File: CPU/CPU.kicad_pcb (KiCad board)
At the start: 2 copper layers, 157.1 x 85.3 mm, 88 parts, among them J101 Conn_02x10_Odd_Even, J102 Conn_02x14_Odd_Even_MountingP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, J301 Conn_02x03_Odd_Even, J302 1X4SMD-FPC, J303 Conn_02x03_Odd_Even, Q101 IRLML0040TR, Q102 IRLML0040TR, Q201 DMC4050, Q301 IRLML0040TR, Q302 IRLML0040TR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

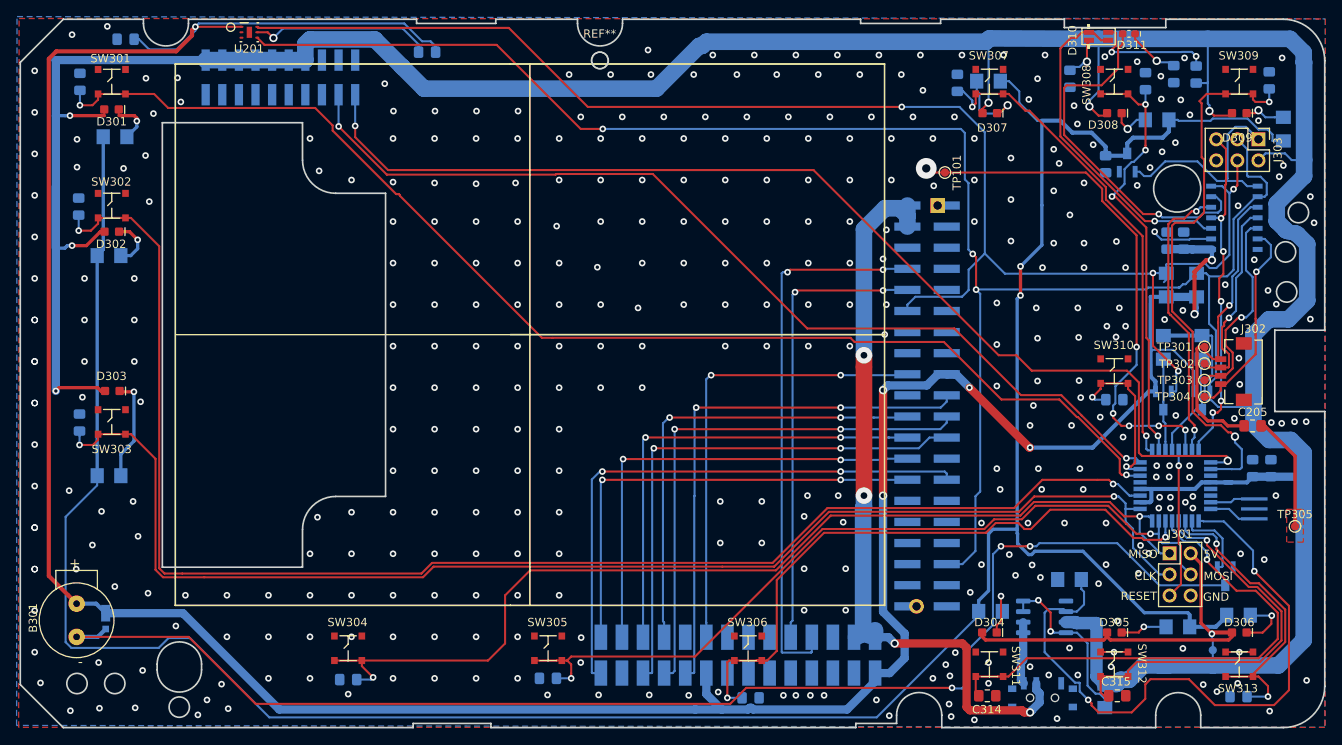
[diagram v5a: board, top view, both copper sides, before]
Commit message: Updates from CPU v1 were completed. Switched out Tiny84 for a tiny1614 because the 84 lacks a hardware twi driver. This version was sent to production at jlcpcb.
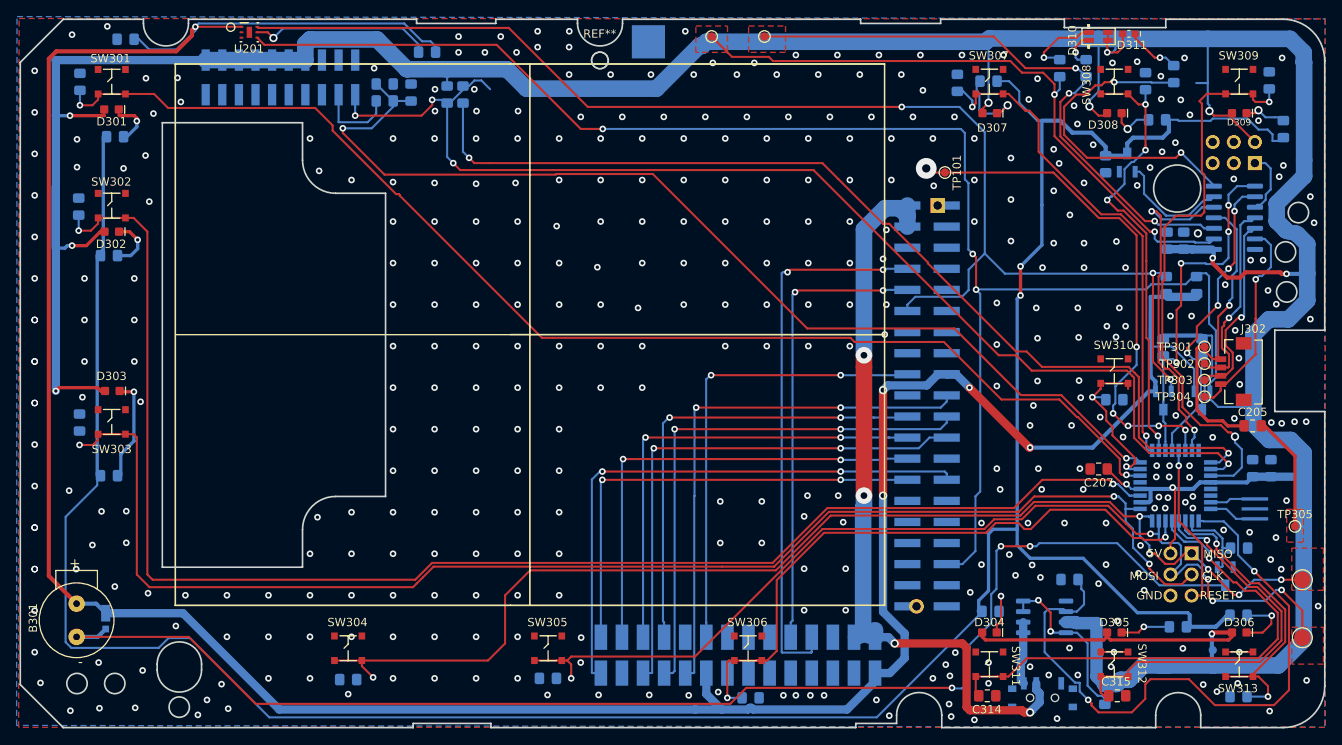
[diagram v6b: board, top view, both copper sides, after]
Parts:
- added C206: 100pF, Capacitor_SMD:C_0805_2012Metric_Pad1.15x1.40mm_HandSolder, B.Cu at (77.5, 54.4)
- added C207: 100nF, Capacitor_SMD:C_0805_2012Metric_Pad1.15x1.40mm_HandSolder, F.Cu at (160.3, 99.7)
- added D201: Schottky, Diode_SMD:D_0805_2012Metric_Pad1.15x1.40mm_HandSolder, B.Cu at (74.3, 53.3)
- added R202: 390K, Resistor_SMD:R_0805_2012Metric_Pad1.15x1.40mm_HandSolder, B.Cu at (81.8, 54.6)
- added R203: 2K, Resistor_SMD:R_0805_2012Metric_Pad1.15x1.40mm_HandSolder, B.Cu at (83.7, 54.6)
- added R204: 1K, Resistor_SMD:R_0805_2012Metric_Pad1.15x1.40mm_HandSolder, B.Cu at (74.3, 55.4)
- added R205: 10K, Resistor_SMD:R_0805_2012Metric_Pad1.15x1.40mm_HandSolder, B.Cu at (177.2, 109.2)
- added RX301: TestPoint, TestPoint:TestPoint_Pad_D1.0mm, F.Cu at (120.0, 47.6)
- added TP201: TestPoint, TestPoint:TestPoint_Pad_4.0x4.0mm, B.Cu at (106.0, 48.3)
- added TPRX201: TestPoint, TestPoint:TestPoint_Pad_D2.0mm, F.Cu at (184.8, 113.0)
- added TPTX201: TestPoint, TestPoint:TestPoint_Pad_D2.0mm, F.Cu at (184.8, 120.0)
- added TX301: TestPoint, TestPoint:TestPoint_Pad_D1.0mm, F.Cu at (113.7, 47.6)
- J301, J303: moved to B.Cu
- R101, R102, R103, R104, R208, R209, R301, R302, R303, R304, R305, R306, R307, R308, R309: footprint CPU:R1206 -> Resistor_SMD:R_0805_2012Metric_Pad1.15x1.40mm_HandSolder
- U202: value ATTINY84ATTINY84-20PU -> ATtiny1614-SS; footprint MarcoK:14SOIC -> Package_SO:SOIC-14_3.9x8.7mm_P1.27mm
- moved R310 16.4 mm to (155.6, 51.4), turned to 90 degrees
- moved J303 2.90 mm to (179.1, 62.9), turned to 90 degrees
- moved J301 2.65 mm to (171.4, 109.9), turned to 180 degrees
- moved R311 2.33 mm to (158.8, 51.4)
- moved Y301 0.07 mm to (179.1, 104.5)
- turned U202 to 0 degrees
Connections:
- C202 pad 1: +3V3 -> 5V
- C203 pad 2: +3V3 -> 5V
- C306 pad 1: GND -> Net-(C306-Pad1)
- C306 pad 2: /Micro Controller Devices/SW- -> Net-(C306-Pad2)
- C307 pad 1: GND -> Net-(C307-Pad1)
- C307 pad 2: /Micro Controller Devices/SWA -> Net-(C307-Pad2)
- C308 pad 1: GND -> Net-(C308-Pad1)
- C308 pad 2: /Micro Controller Devices/SWB -> Net-(C308-Pad2)
- J303 pad 1: /I2C Devices/LED_PWM -> /I2C Devices/UPDI
- J303 pad 3: /SCL -> Net-(J303-Pad3)
- J303 pad 4: /SDA -> Net-(J303-Pad4)
- J303 pad 5: /I2C Devices/85RES -> Net-(J303-Pad5)
- R310 pad 1: /I2C Devices/GREEN -> /I2C Devices/RED
- R311 pad 2: /I2C Devices/RED -> /I2C Devices/GREEN
- U202 pad 1: +3V3 -> 5V
- U202 pad 10: /I2C Devices/SCC -> /I2C Devices/UPDI
- U202 pad 2: /I2C Devices/GREEN -> /I2C Devices/RED
- U202 pad 3: /I2C Devices/RED -> /I2C Devices/GREEN
- U202 pad 4: /I2C Devices/85RES -> /I2C Devices/SCC
- U202 pad 6: /I2C Devices/ORANGE -> /I2C Devices/LED_PWM
- U202 pad 7: /SDA -> /I2C Devices/ORANGE
- U202 pad 8: /I2C Devices/LED_PWM -> /SDA5
- U202 pad 9: /SCL -> /SCL5
- U301 pad 1: /CH_STAT -> Net-(R203-Pad2)
- U301 pad 2: /Micro Controller Devices/SWM -> /CH_STAT
- U301 pad 24: +BATT -> /Micro Controller Devices/BATT_V
- U301 pad 3: Net-(U301-Pad3) -> /Micro Controller Devices/SWM
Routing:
- net /Micro Controller Devices/BATT_V: track 0.00 -> 125.7 mm, vias 0 -> 2
- net Net-(R203-Pad2): track 0.00 -> 120.0 mm, vias 0 -> 2
- net +BATT: track 116.9 -> 9.80 mm, vias 2 -> 0
- net /I2C Devices/RED: track 0.00 -> 77.7 mm, vias 0 -> 2
- net /I2C Devices/GREEN: track 7.31 -> 72.3 mm, vias 1 -> 3
- net /I2C Devices/85RES: track 41.7 -> 0.00 mm, vias 5 -> 0
- net /I2C Devices/R_G: track 40.3 -> 0.00 mm, vias 1 -> 0
- net /SDA5: track 11.1 -> 42.3 mm, vias 0 -> 4
- net 5V: track 480.2 -> 511.1 mm, vias 7 -> 12
- net /SDA: track 185.4 -> 159.6 mm, vias 4 -> 3
- net /SCL5: track 13.0 -> 38.4 mm, vias 0 -> 4
- net /SCL: track 212.6 -> 189.0 mm
- net /Micro Controller Devices/SWB: track 97.8 -> 120.5 mm, vias 2 -> 5
- net /Micro Controller Devices/SWA: track 122.0 -> 140.6 mm, vias 2 -> 6
- net +3V3: track 363.0 -> 346.7 mm, vias 7 -> 5
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- added copper zone on F.Cu, net /I2C Devices/GREEN
- added copper zone on F.Cu, net /I2C Devices/RED
- added copper zone on F.Cu, net /Micro Controller Devices/SWA
- added copper zone on F.Cu, net /Micro Controller Devices/SWB
